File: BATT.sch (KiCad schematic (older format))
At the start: 10 parts

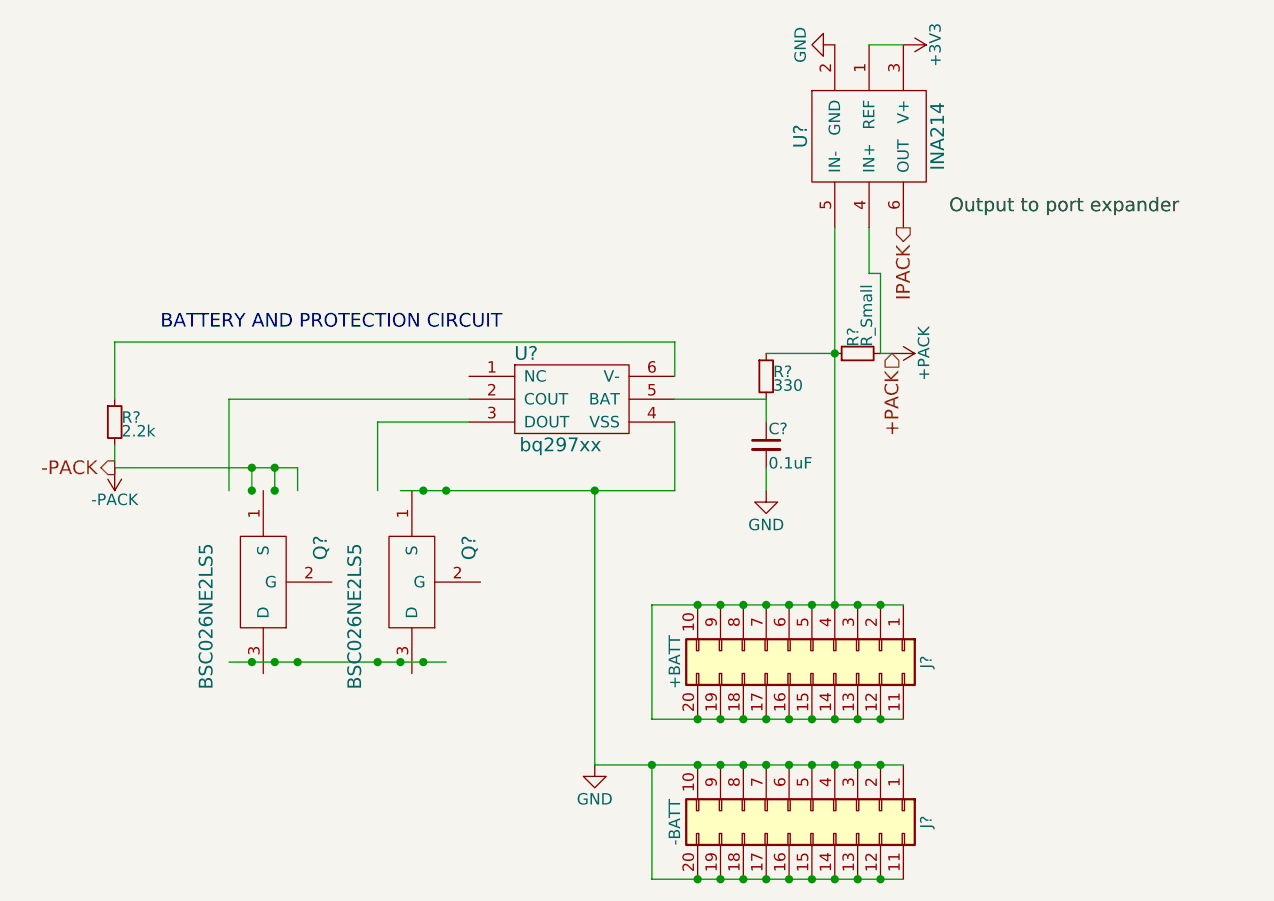
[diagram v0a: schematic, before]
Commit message: Began interfacing with µC
Also all 9V should now be 5V, change resistors accordingly.
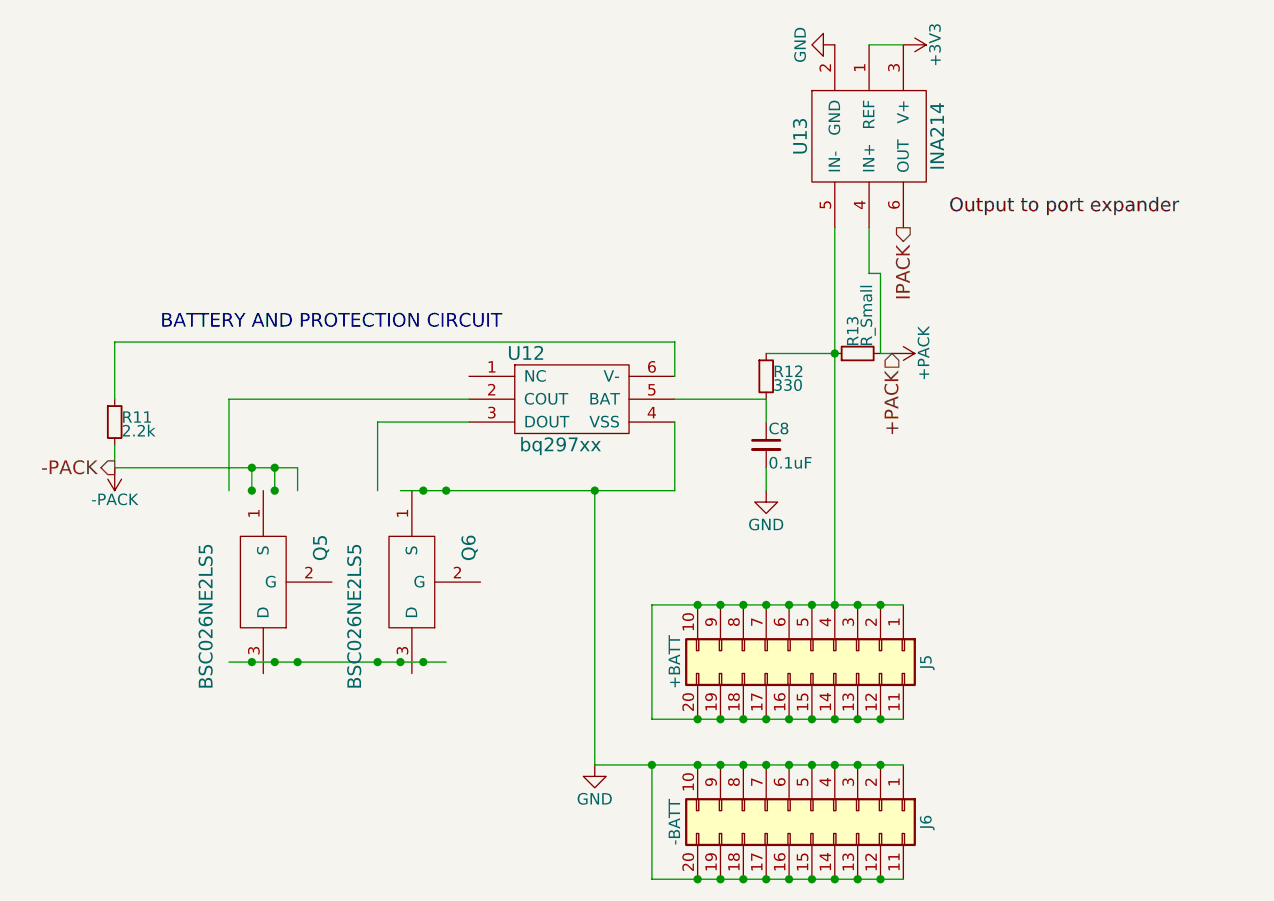
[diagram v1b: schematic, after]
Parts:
- gave numbers to parts that had none: 10
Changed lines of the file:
@@
 LIBS:ina214
 LIBS:tps61088
+LIBS:cdh_lib
 LIBS:eps_v1-cache
 EELAYER 25 0
@@
 $EndDescr
 $Comp
-L bq297xx U?
+L bq297xx U12
 U 1 1 59EA5293
 P 5650 2750
-F 0 "U?" H 5450 2950 60  0000 C CNN
+F 0 "U12" H 5450 2950 60  0000 C CNN
 F 1 "bq297xx" H 5600 2550 60  0000 C CNN
 F 2 "" H 5500 2450 60  0001 C CNN
@@
 $EndComp
 $Comp
-L BSC026NE2LS5 Q?
+L BSC026NE2LS5 Q5
 U 1 1 59EA52A1
 P 4300 3550
-F 0 "Q?" H 4150 3800 60  0000 C CNN
+F 0 "Q5" H 4150 3800 60  0000 C CNN
 F 1 "BSC026NE2LS5" H 4450 3300 60  0000 C CNN
 F 2 "" H 4300 3550 60  0001 C CNN
@@
 $EndComp
 $Comp
-L BSC026NE2LS5 Q?
+L BSC026NE2LS5 Q6
 U 1 1 59EA52A8
 P 4950 3550
-F 0 "Q?" H 4800 3800 60  0000 C CNN
+F 0 "Q6" H 4800 3800 60  0000 C CNN
 F 1 "BSC026NE2LS5" H 5100 3300 60  0000 C CNN
 F 2 "" H 4950 3550 60  0001 C CNN
@@
 $EndComp
 $Comp
-L R_Small R?
+L R_Small R11
 U 1 1 59EA52AF
 P 3650 2850
-F 0 "R?" H 3680 2870 50  0000 L CNN
+F 0 "R11" H 3680 2870 50  0000 L CNN
 F 1 "2.2k" H 3680 2810 50  0000 L CNN
 F 2 "" H 3650 2850 50  0001 C CNN
@@
 $EndComp
 $Comp
-L C_Small C?
+L C_Small C8
 U 1 1 59EA52BD
 P 6500 2950
-F 0 "C?" H 6510 3020 50  0000 L CNN
+F 0 "C8" H 6510 3020 50  0000 L CNN
 F 1 "0.1uF" H 6510 2870 50  0000 L CNN
 F 2 "" H 6500 2950 50  0001 C CNN
@@
 $EndComp
 $Comp
-L +PACK #PWR054
+L +PACK #PWR58
 U 1 1 59EA52CA
 P 7050 2550
-F 0 "#PWR054" H 7050 2400 50  0001 C CNN
+F 0 "#PWR58" H 7050 2400 50  0001 C CNN
 F 1 "+PACK" H 7050 2690 50  0000 C CNN
 F 2 "" H 7050 2550 50  0001 C CNN
@@
 +PACK
 $Comp
-L INA214 U?
+L INA214 U13
 U 1 1 5A10F7B5
 P 6950 1600
-F 0 "U?" H 6950 1300 60  0000 C CNN
+F 0 "U13" H 6950 1300 60  0000 C CNN
 F 1 "INA214" H 6950 1900 60  0000 C CNN
 F 2 "" H 6950 1900 60  0001 C CNN
@@
 $EndComp
 $Comp
-L R_Small R?
+L R_Small R13
 U 1 1 5A112EB5
 P 6900 2550
-F 0 "R?" H 6930 2570 50  0000 L CNN
+F 0 "R13" H 6930 2570 50  0000 L CNN
 F 1 "R_Small" H 6930 2510 50  0000 L CNN
 F 2 "" H 6900 2550 50  0001 C CNN
@@
 $EndComp
 $Comp
-L +3V3 #PWR055
+L +3V3 #PWR59
 U 1 1 5A113C8A
 P 7100 1200
-F 0 "#PWR055" H 7100 1050 50  0001 C CNN
+F 0 "#PWR59" H 7100 1050 50  0001 C CNN
 F 1 "+3V3" H 7100 1340 50  0000 C CNN
 F 2 "" H 7100 1200 50  0001 C CNN
@@
 $EndComp
 $Comp
-L GND #PWR056
+L GND #PWR57
 U 1 1 5A113CE6
 P 6800 1200
-F 0 "#PWR056" H 6800 950 50  0001 C CNN
+F 0 "#PWR57" H 6800 950 50  0001 C CNN
 F 1 "GND" H 6800 1050 50  0000 C CNN
 F 2 "" H 6800 1200 50  0001 C CNN
@@
 Output to port expander
 $Comp
-L Conn_02x10_Top_Bottom J?
+L Conn_02x10_Top_Bottom J6
 U 1 1 5A4805FA
 P 6700 4550
-F 0 "J?" H 6750 5050 50  0000 C CNN
+F 0 "J6" H 6750 5050 50  0000 C CNN
 F 1 "-BATT" H 6750 3950 50  0000 C CNN
 F 2 "" H 6700 4550 50  0001 C CNN
@@
 $EndComp
 $Comp
-L Conn_02x10_Top_Bottom J?
+L Conn_02x10_Top_Bottom J5
 U 1 1 5A480EC8
 P 6700 3850
-F 0 "J?" H 6750 4350 50  0000 C CNN
+F 0 "J5" H 6750 4350 50  0000 C CNN
 F 1 "+BATT" H 6750 3250 50  0000 C CNN
 F 2 "" H 6700 3850 50  0001 C CNN
@@
 $EndComp
 $Comp
-L GND #PWR057
+L GND #PWR55
 U 1 1 5A481828
 P 5750 4350
-F 0 "#PWR057" H 5750 4100 50  0001 C CNN
+F 0 "#PWR55" H 5750 4100 50  0001 C CNN
 F 1 "GND" H 5750 4200 50  0000 C CNN
 F 2 "" H 5750 4350 50  0001 C CNN
@@
 $EndComp
 $Comp
-L GND #PWR058
+L GND #PWR56
 U 1 1 5A481904
 P 6500 3150
-F 0 "#PWR058" H 6500 2900 50  0001 C CNN
+F 0 "#PWR56" H 6500 2900 50  0001 C CNN
 F 1 "GND" H 6500 3000 50  0000 C CNN
 F 2 "" H 6500 3150 50  0001 C CNN
@@
 Connection ~ 6000 4350
 $Comp
-L R_Small R?
+L R_Small R12
 U 1 1 59EA52B6
 P 6500 2650
-F 0 "R?" H 6530 2670 50  0000 L CNN
+F 0 "R12" H 6530 2670 50  0000 L CNN
 F 1 "330" H 6530 2610 50  0000 L CNN
 F 2 "" H 6500 2650 50  0001 C CNN
@@
 Connection ~ 5100 3150
 $Comp
-L -PACK #PWR059
+L -PACK #PWR54
 U 1 1 5A48370F
 P 3650 3050
-F 0 "#PWR059" H 3650 2900 50  0001 C CNN
+F 0 "#PWR54" H 3650 2900 50  0001 C CNN
 F 1 "-PACK" H 3650 3190 50  0000 C CNN
 F 2 "" H 3650 3050 50  0001 C CNN

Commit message: PCB layout as of 2018-02-07
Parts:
- Q5, Q6: footprint (none) -> Housings_SON:VSONP-8-1EP_5x6_Pitch1.27mm
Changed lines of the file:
@@
 F 0 "Q5" H 4150 3800 60  0000 C CNN
 F 1 "BSC026NE2LS5" H 4450 3300 60  0000 C CNN
-F 2 "" H 4300 3550 60  0001 C CNN
+F 2 "Housings_SON:VSONP-8-1EP_5x6_Pitch1.27mm" H 4300 3550 60  0001 C CNN
 F 3 "" H 4300 3550 60  0001 C CNN
 	1    4300 3550
@@
 F 0 "Q6" H 4800 3800 60  0000 C CNN
 F 1 "BSC026NE2LS5" H 5100 3300 60  0000 C CNN
-F 2 "" H 4950 3550 60  0001 C CNN
+F 2 "Housings_SON:VSONP-8-1EP_5x6_Pitch1.27mm" H 4950 3550 60  0001 C CNN
 F 3 "" H 4950 3550 60  0001 C CNN
 	1    4950 3550
@@
 $EndComp
 $Comp
-L +PACK #PWR58
+L +PACK #PWR070
 U 1 1 59EA52CA
 P 7050 2550
-F 0 "#PWR58" H 7050 2400 50  0001 C CNN
+F 0 "#PWR070" H 7050 2400 50  0001 C CNN
 F 1 "+PACK" H 7050 2690 50  0000 C CNN
 F 2 "" H 7050 2550 50  0001 C CNN
@@
 $EndComp
 $Comp
-L +3V3 #PWR59
+L +3V3 #PWR071
 U 1 1 5A113C8A
 P 7100 1200
-F 0 "#PWR59" H 7100 1050 50  0001 C CNN
+F 0 "#PWR071" H 7100 1050 50  0001 C CNN
 F 1 "+3V3" H 7100 1340 50  0000 C CNN
 F 2 "" H 7100 1200 50  0001 C CNN
@@
 $EndComp
 $Comp
-L GND #PWR57
+L GND #PWR072
 U 1 1 5A113CE6
 P 6800 1200
-F 0 "#PWR57" H 6800 950 50  0001 C CNN
+F 0 "#PWR072" H 6800 950 50  0001 C CNN
 F 1 "GND" H 6800 1050 50  0000 C CNN
 F 2 "" H 6800 1200 50  0001 C CNN
@@
 $EndComp
 $Comp
-L GND #PWR55
+L GND #PWR073
 U 1 1 5A481828
 P 5750 4350
-F 0 "#PWR55" H 5750 4100 50  0001 C CNN
+F 0 "#PWR073" H 5750 4100 50  0001 C CNN
 F 1 "GND" H 5750 4200 50  0000 C CNN
 F 2 "" H 5750 4350 50  0001 C CNN
@@
 $EndComp
 $Comp
-L GND #PWR56
+L GND #PWR074
 U 1 1 5A481904
 P 6500 3150
-F 0 "#PWR56" H 6500 2900 50  0001 C CNN
+F 0 "#PWR074" H 6500 2900 50  0001 C CNN
 F 1 "GND" H 6500 3000 50  0000 C CNN
 F 2 "" H 6500 3150 50  0001 C CNN
@@
 Connection ~ 5100 3150
 $Comp
-L -PACK #PWR54
+L -PACK #PWR075
 U 1 1 5A48370F
 P 3650 3050
-F 0 "#PWR54" H 3650 2900 50  0001 C CNN
+F 0 "#PWR075" H 3650 2900 50  0001 C CNN
 F 1 "-PACK" H 3650 3190 50  0000 C CNN
 F 2 "" H 3650 3050 50  0001 C CNN

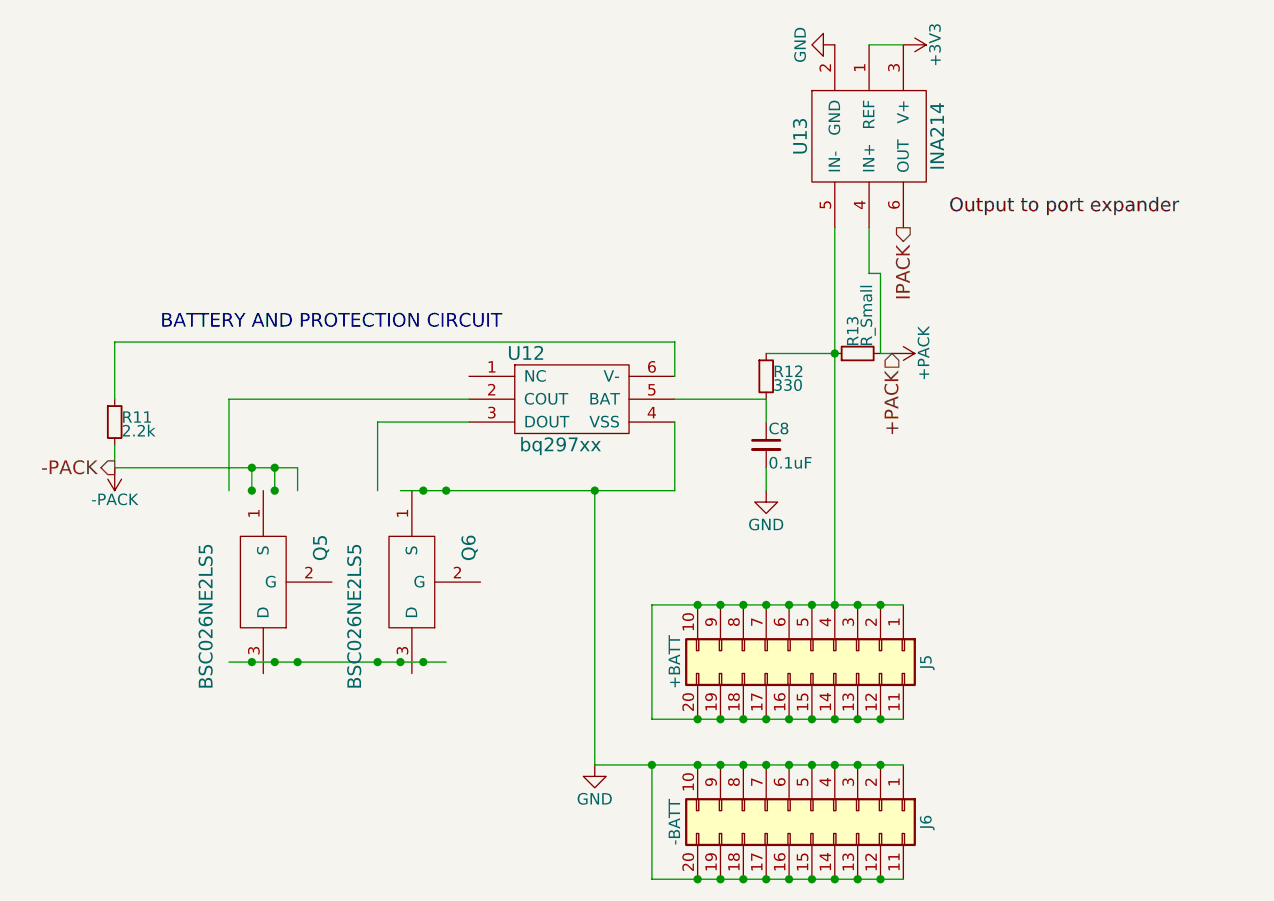
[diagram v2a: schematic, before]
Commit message: PCB layout as of 2018-02-12
All that’s left to do is add deployment switches
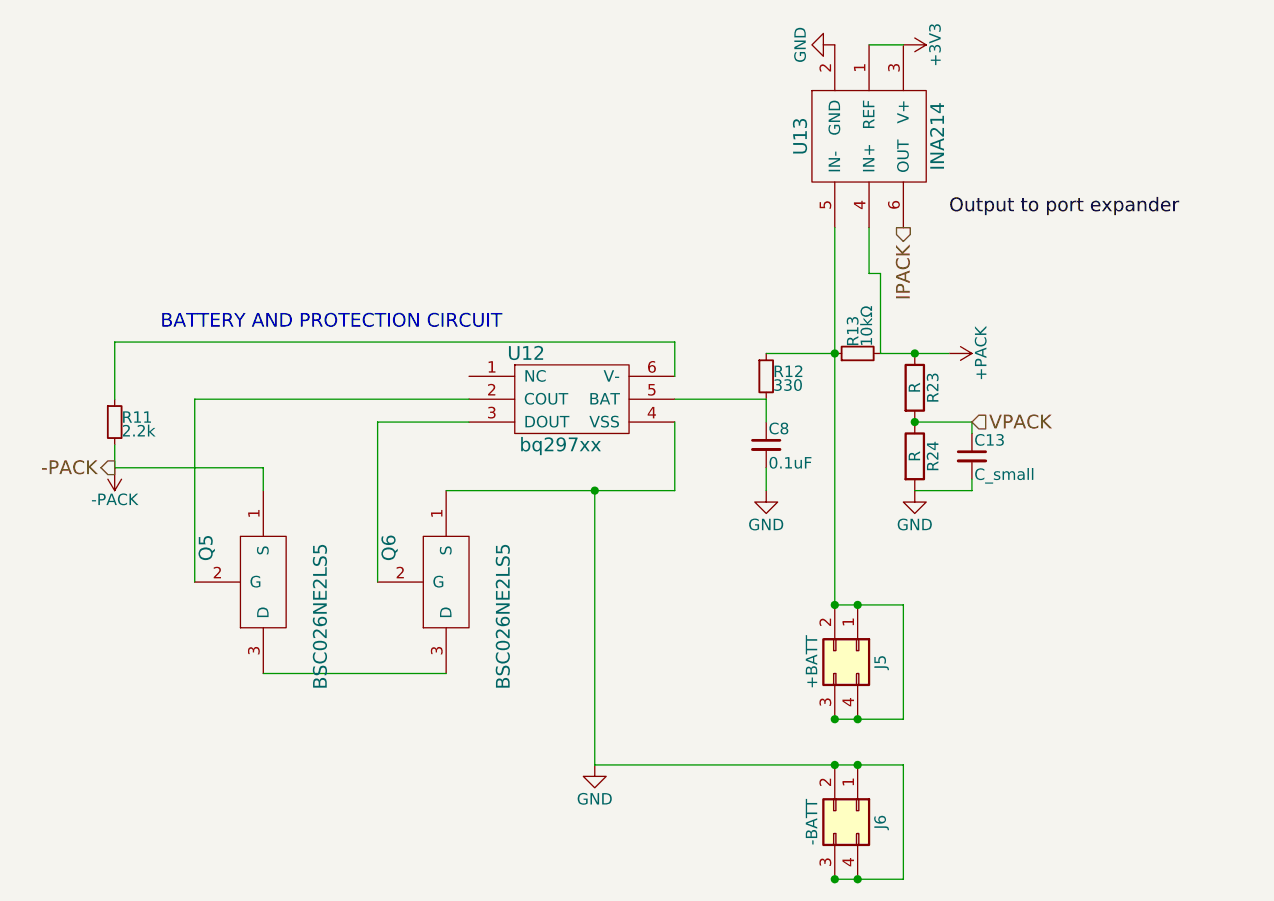
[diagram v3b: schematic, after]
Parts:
- removed J5: +BATT, symbol Conn_02x10_Top_Bottom
- removed J6: -BATT, symbol Conn_02x10_Top_Bottom
- added C13: C_small, Capacitors_SMD:C_0603_HandSoldering, symbol C_Small
- added J5: +BATT, Pin_Headers:Pin_Header_Straight_2x02_Pitch2.54mm, symbol Conn_02x02_Counter_Clockwise
- added J6: -BATT, Pin_Headers:Pin_Header_Straight_2x02_Pitch2.54mm, symbol Conn_02x02_Counter_Clockwise
- added R23, R24: R, Resistors_SMD:R_0603_HandSoldering, symbol R
- C8: footprint (none) -> Capacitors_SMD:C_0603_HandSoldering
- R11, R12: footprint (none) -> Resistors_SMD:R_0603_HandSoldering
- R13: value R_Small -> 10kΩ; footprint (none) -> Resistors_SMD:R_0603_HandSoldering
- U12: footprint (none) -> Housings_SON:WSON6_1.5x1.5mm_Pitch0.5mm
- U13: footprint (none) -> kicad-libraries:SC70-6
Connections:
- net labels added: VPACK
- wire segments 32 -> 34
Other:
- moved on the sheet: Q5, Q6

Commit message: Added deployment/RBL switches and debug headers to EPS board
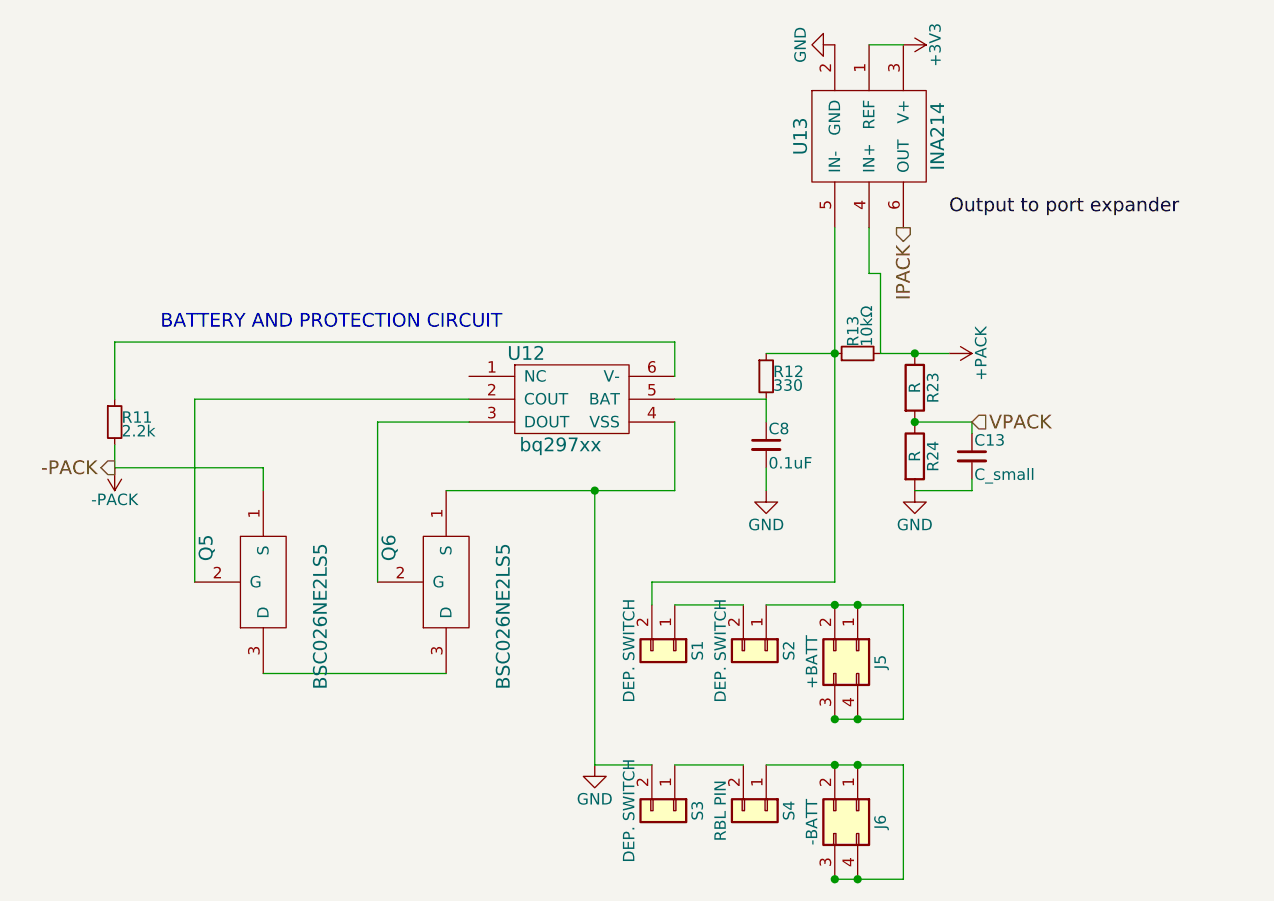
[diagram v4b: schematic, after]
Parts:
- added S1, S2, S3: DEP. SWITCH, Connectors_Hirose:Hirose_DF13-02P-1.25DS_02x1.25mm_Angled, symbol Conn_01x02
- added S4: RBL PIN, Connectors_Hirose:Hirose_DF13-02P-1.25DS_02x1.25mm_Angled, symbol Conn_01x02
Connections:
- net GND: now also S3.2 (Pin_2); no longer J6.1 (Pin_1), J6.2 (Pin_2), J6.3 (Pin_3), J6.4 (Pin_4)
- net at J5.1 (Pin_1), J5.2 (Pin_2), J5.3 (Pin_3)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: now also S2.1 (Pin_1); no longer R12.1, R13.1, U13.5 (IN-)
- new net: R12.1, R13.1, S1.2 (Pin_2), U13.5 (IN-)
- new net: J6.1 (Pin_1), J6.2 (Pin_2), J6.3 (Pin_3), J6.4 (Pin_4), S4.1 (Pin_1)
- new net: S3.1 (Pin_1), S4.2 (Pin_2)
- new net: S1.1 (Pin_1), S2.2 (Pin_2)
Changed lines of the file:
@@
 	6950 1200 7100 1200
-Wire Wire Line
-	6800 2000 6800 3650
 Wire Wire Line
 	6500 2550 6800 2550
@@
 Connection ~ 6900 4150
 Connection ~ 6800 4150
-Wire Wire Line
-	5750 4350 7100 4350
 Connection ~ 6900 4350
 Connection ~ 6800 4350
@@
 $EndComp
 Wire Wire Line
-	6800 3650 7100 3650
+	6500 3650 7100 3650
 Wire Wire Line
 	6800 4150 7100 4150
@@
 Connection ~ 6900 4850
 Connection ~ 6800 4850
+$Comp
+L Conn_01x02 S3
+U 1 1 5A84F4B4
+P 6100 4550
+F 0 "S3" H 6100 4650 50  0000 C CNN
+F 1 "DEP. SWITCH" H 6100 4350 50  0000 C CNN
+F 2 "Connectors_Hirose:Hirose_DF13-02P-1.25DS_02x1.25mm_Angled" H 6100 4550 50  0001 C CNN
+F 3 "" H 6100 4550 50  0001 C CNN
+	1    6100 4550
+	0    1    1    0
+$EndComp
+$Comp
+L Conn_01x02 S4
+U 1 1 5A84F546
+P 6500 4550
+F 0 "S4" H 6500 4650 50  0000 C CNN
+F 1 "RBL PIN" H 6500 4350 50  0000 C CNN
+F 2 "Connectors_Hirose:Hirose_DF13-02P-1.25DS_02x1.25mm_Angled" H 6500 4550 50  0001 C CNN
+F 3 "" H 6500 4550 50  0001 C CNN
+	1    6500 4550
+	0    1    1    0
+$EndComp
+Wire Wire Line
+	6500 4350 7100 4350
+Wire Wire Line
+	6400 4350 6100 4350
+Wire Wire Line
+	5750 4350 6000 4350
+$Comp
+L Conn_01x02 S1
+U 1 1 5A84FC22
+P 6100 3850
+F 0 "S1" H 6100 3950 50  0000 C CNN
+F 1 "DEP. SWITCH" H 6100 3650 50  0000 C CNN
+F 2 "Connectors_Hirose:Hirose_DF13-02P-1.25DS_02x1.25mm_Angled" H 6100 3850 50  0001 C CNN
+F 3 "" H 6100 3850 50  0001 C CNN
+	1    6100 3850
+	0    1    1    0
+$EndComp
+$Comp
+L Conn_01x02 S2
+U 1 1 5A84FC29
+P 6500 3850
+F 0 "S2" H 6500 3950 50  0000 C CNN
+F 1 "DEP. SWITCH" H 6500 3650 50  0000 C CNN
+F 2 "Connectors_Hirose:Hirose_DF13-02P-1.25DS_02x1.25mm_Angled" H 6500 3850 50  0001 C CNN
+F 3 "" H 6500 3850 50  0001 C CNN
+	1    6500 3850
+	0    1    1    0
+$EndComp
+Wire Wire Line
+	6800 2000 6800 3550
+Wire Wire Line
+	6400 3650 6100 3650
+Wire Wire Line
+	6000 3650 6000 3550
+Wire Wire Line
+	6000 3550 6800 3550
 $EndSCHEMATC

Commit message: Exported EPS board
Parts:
- J5, J6: footprint Pin_Headers:Pin_Header_Straight_2x02_Pitch2.54mm -> Connectors_Hirose:Hirose_DF13-04P-1.25DS_04x1.25mm_Angled
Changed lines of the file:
@@
 F 0 "J5" H 6950 3950 50  0000 C CNN
 F 1 "+BATT" H 6950 3650 50  0000 C CNN
-F 2 "Pin_Headers:Pin_Header_Straight_2x02_Pitch2.54mm" H 6900 3850 50  0001 C CNN
+F 2 "Connectors_Hirose:Hirose_DF13-04P-1.25DS_04x1.25mm_Angled" H 6900 3850 50  0001 C CNN
 F 3 "" H 6900 3850 50  0001 C CNN
 	1    6900 3850
@@
 F 0 "J6" H 6950 4650 50  0000 C CNN
 F 1 "-BATT" H 6950 4350 50  0000 C CNN
-F 2 "Pin_Headers:Pin_Header_Straight_2x02_Pitch2.54mm" H 6900 4550 50  0001 C CNN
+F 2 "Connectors_Hirose:Hirose_DF13-04P-1.25DS_04x1.25mm_Angled" H 6900 4550 50  0001 C CNN
 F 3 "" H 6900 4550 50  0001 C CNN
 	1    6900 4550
